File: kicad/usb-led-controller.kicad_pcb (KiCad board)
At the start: 4 copper layers, 70 x 30 mm, 109 parts, among them J1 SWD, J2 PWR, J3 USB, J4 PWM_0, J5 PWM_1, J6 WS2812_0, J7 WS2812_1, Q1 NVS4409N, Q2 NVS4409N, Q3 NVS4409N, Q4 NVS4409N, Q5 NVS4409N, Q6 NVS4409N, U1 SN74LV1T125, U2 SN74LV1T125, U3 STM32F042F6Px, U4 MIC5501-XYM5, U5 USBLC6, U6 SN74LVC1G04

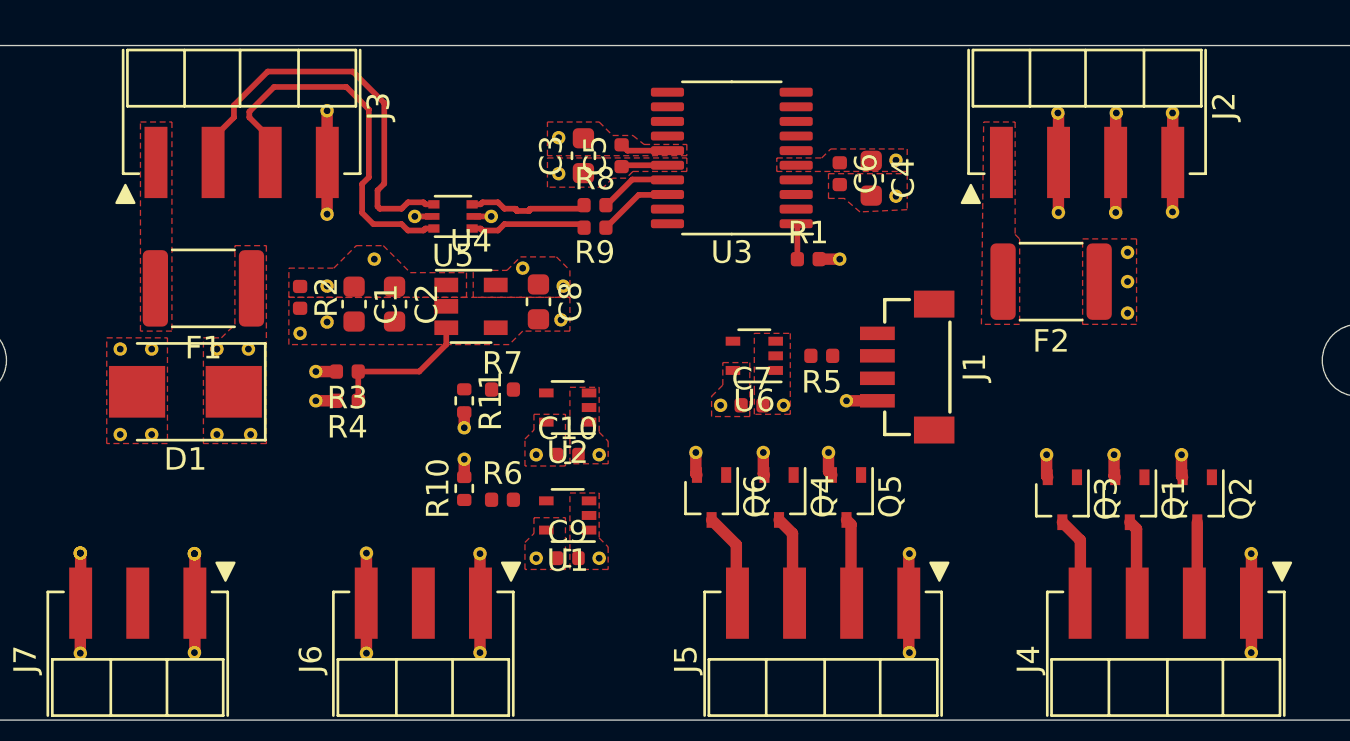
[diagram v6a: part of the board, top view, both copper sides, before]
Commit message: Cmopleted initial routing
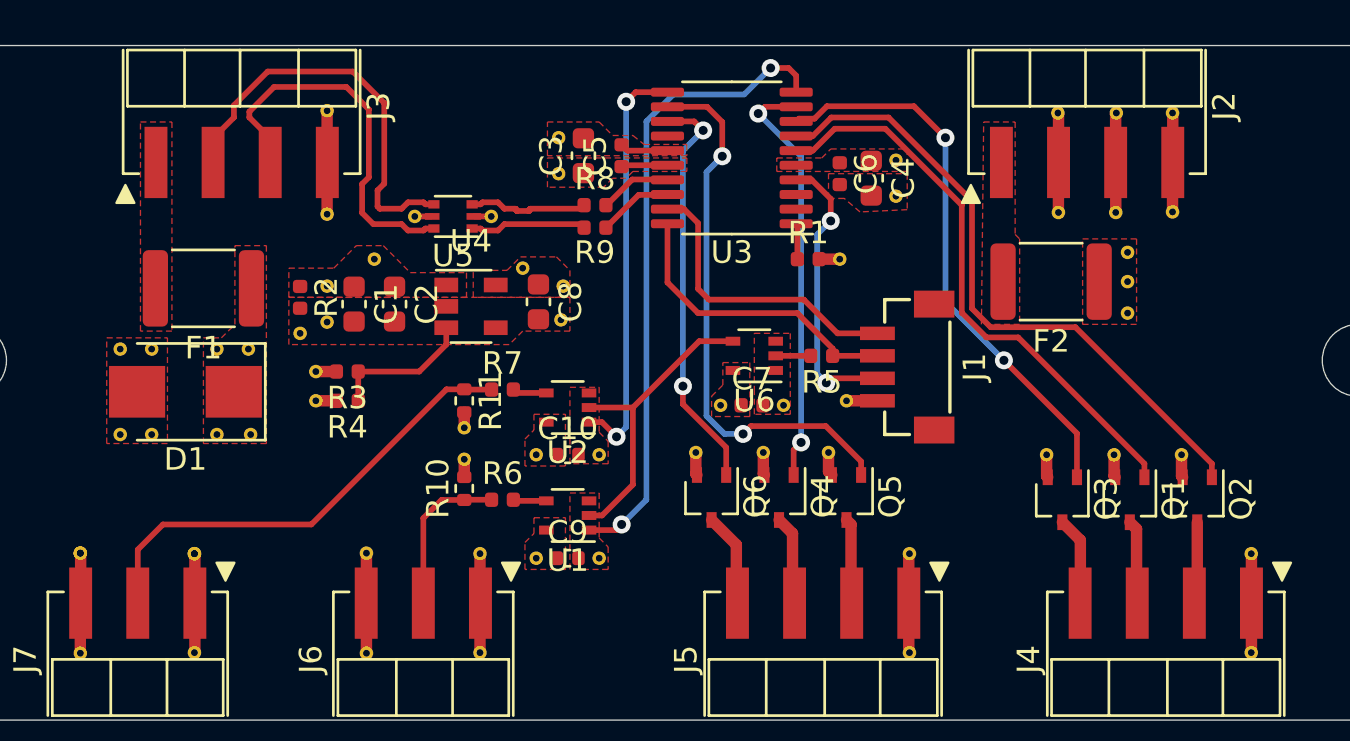
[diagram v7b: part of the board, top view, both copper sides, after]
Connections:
- R11 pad 1: /WS2812_1_DATA_R -> /WS2812_1_DATA
- R7 pad 1: /WS2812_1_DATA_R -> /WS2812_1_DATA
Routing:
- net /GATE_0_G: track 0.00 -> 28.6 mm
- net /WS2812_0_~OE: track 0.00 -> 28.5 mm, vias 0 -> 2
- net /GATE_0_R: track 0.00 -> 25.5 mm
- net /GATE_0_B: track 0.00 -> 25.0 mm, vias 0 -> 2
- net /GATE_1_G: track 0.00 -> 24.7 mm, vias 0 -> 2
- net /WS2812_1_DATA: track 0.00 -> 21.1 mm
- net /GATE_1_R: track 0.00 -> 18.8 mm, vias 0 -> 2
- net /WS2812_1_~OE: track 0.00 -> 18.6 mm, vias 0 -> 2
- net /GATE_1_B: track 0.00 -> 18.2 mm, vias 0 -> 2
- net /WS2812_DATA_INV: track 0.00 -> 13.6 mm
- net /SWCLK: track 0.00 -> 13.5 mm
- net /SWDIO: track 0.00 -> 13.3 mm
- net /NRST: track 0.00 -> 12.8 mm, vias 0 -> 2
- net /WS2812_0_DATA: track 0.00 -> 7.15 mm
- net /WS2812_DATA: track 0.00 -> 1.56 mm
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
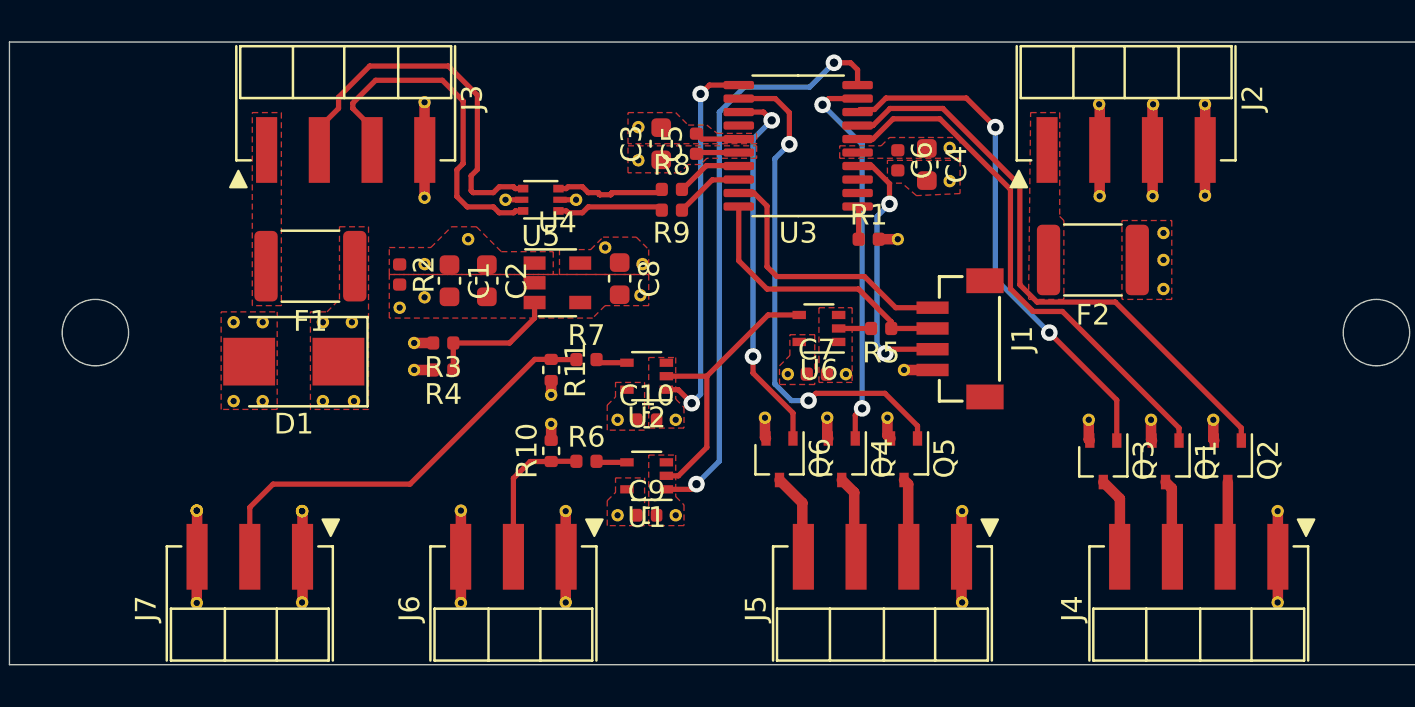
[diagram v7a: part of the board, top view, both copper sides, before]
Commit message: Cleaning up silkscreen
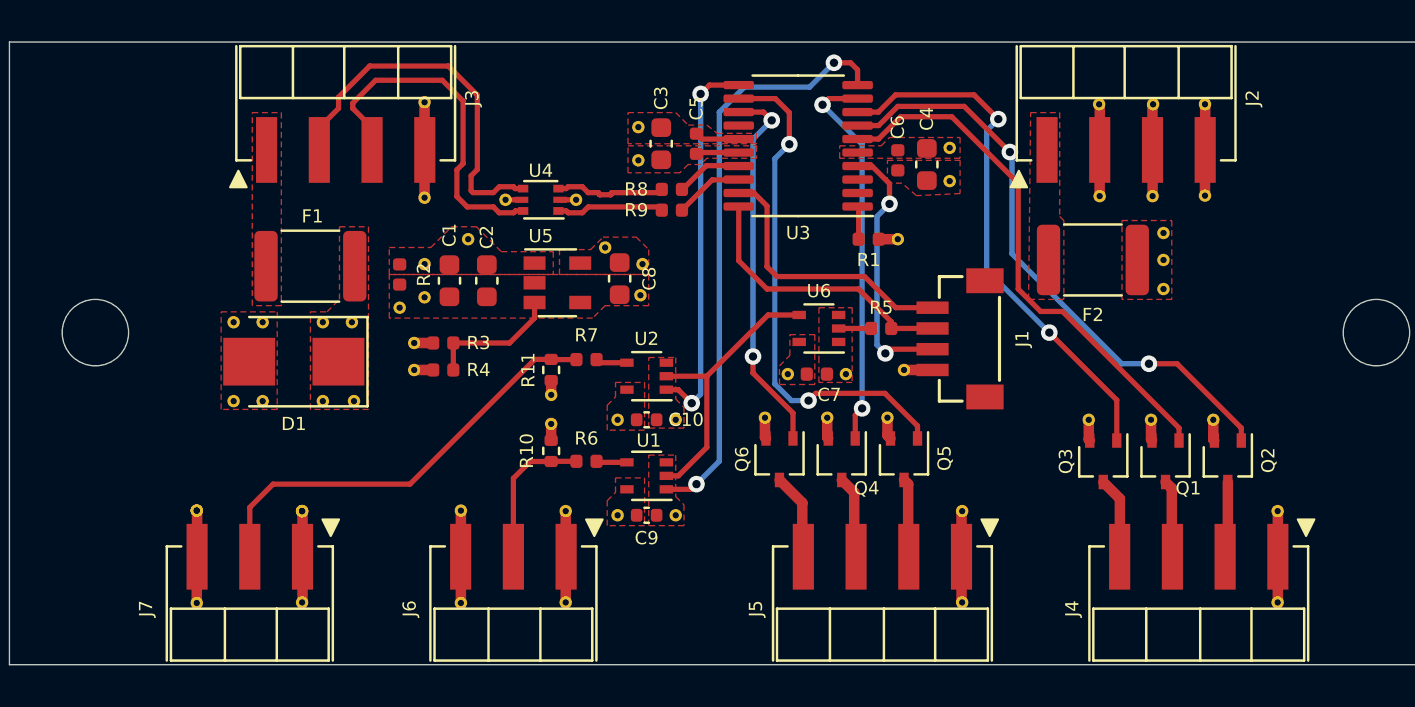
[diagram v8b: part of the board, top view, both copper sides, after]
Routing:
- net /GATE_0_B: track 25.0 -> 25.9 mm
- net /GATE_0_G: track 28.6 -> 28.7 mm, vias 0 -> 2
